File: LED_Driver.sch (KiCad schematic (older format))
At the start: 0 parts

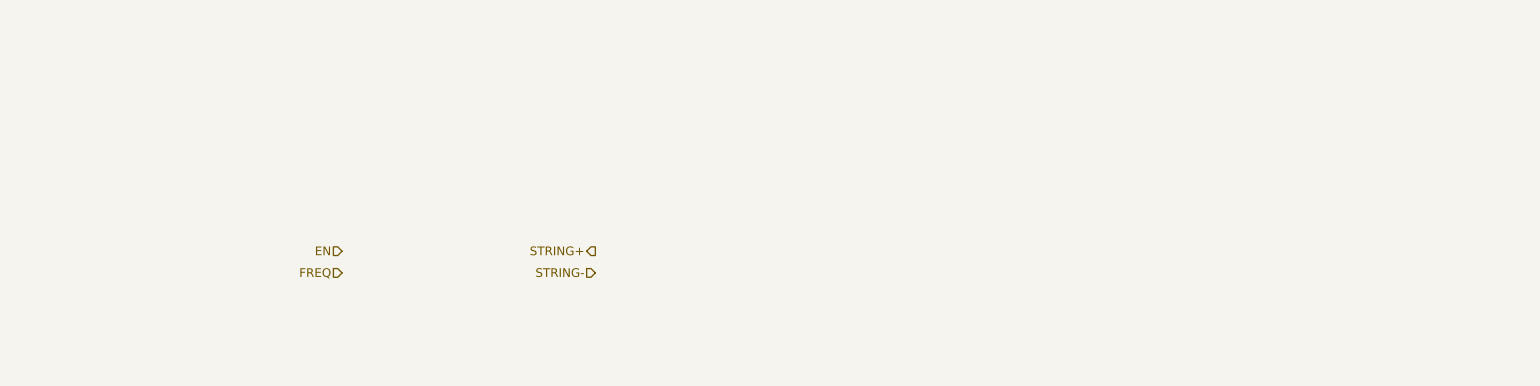
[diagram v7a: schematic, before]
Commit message: WIRED BLOCK DIAGRAM TOGETHER AND ADDED ARDUINO BLOCK
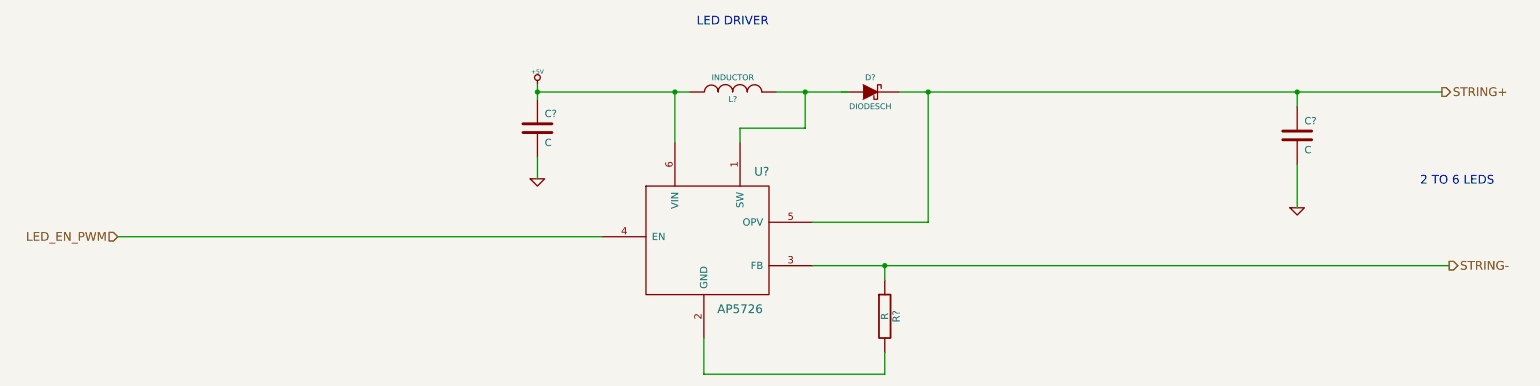
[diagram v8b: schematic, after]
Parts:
- added C? (x2): C, symbol C
- added D?: DIODESCH, symbol DIODESCH
- added L?: INDUCTOR, symbol INDUCTOR
- added R?: R, symbol R
- added U?: AP5726, symbol AP5726
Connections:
- net labels added: +5V, GND, LED_EN_PWM
- net labels removed: EN, FREQ
- wire segments 0 -> 19
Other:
- note added: "2 TO 6 LEDS\n"
- note added: "LED DRIVER"
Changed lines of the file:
@@
-EESchema Schematic File Version 2  date Sat 08 Feb 2014 08:25:16 PM EST
+EESchema Schematic File Version 2  date Sat 08 Feb 2014 11:37:49 PM EST
 LIBS:power
 LIBS:device
@@
 $Descr A4 11700 8267
 encoding utf-8
-Sheet 3 9
+Sheet 2 9
 Title ""
 Date "9 feb 2014"
@@
 Comment4 ""
 $EndDescr
-Text HLabel 4750 3450 0    60   Input ~ 0
+Text Notes 10450 2850 0    60   ~ 0
+2 TO 6 LEDS\n
+Text Notes 5450 1750 0    60   ~ 0
+LED DRIVER
+Wire Wire Line
+	9600 2700 9600 3000
+Connection ~ 6750 3400
+Wire Wire Line
+	6750 3500 6750 3400
+Connection ~ 9600 2200
+Wire Wire Line
+	10600 2200 6850 2200
+Wire Wire Line
+	6250 3100 7050 3100
+Wire Wire Line
+	7050 3100 7050 2200
+Connection ~ 5300 2200
+Wire Wire Line
+	5400 2200 4350 2200
+Connection ~ 4350 2200
+Wire Wire Line
+	5300 2200 5300 2550
+Wire Wire Line
+	4350 2650 4350 2800
+Wire Wire Line
+	1450 3200 4800 3200
+Wire Wire Line
+	4350 2150 4350 2250
+Wire Wire Line
+	5750 2550 5750 2450
+Wire Wire Line
+	5750 2450 6200 2450
+Wire Wire Line
+	6200 2450 6200 2200
+Wire Wire Line
+	6500 2200 6000 2200
+Connection ~ 6200 2200
+Wire Wire Line
+	9600 2200 9600 2300
+Connection ~ 7050 2200
+Wire Wire Line
+	6250 3400 10650 3400
+Wire Wire Line
+	6750 4000 6750 4150
+Wire Wire Line
+	6750 4150 5500 4150
+Wire Wire Line
+	5500 4150 5500 3900
+$Comp
+L C C?
+U 1 1 52F6E658
+P 9600 2500
+F 0 "C?" H 9650 2600 50  0000 L CNN
+F 1 "C" H 9650 2400 50  0000 L CNN
+	1    9600 2500
+	1    0    0    -1
+$EndComp
+$Comp
+L R R?
+U 1 1 52F6E64C
+P 6750 3750
+F 0 "R?" V 6830 3750 50  0000 C CNN
+F 1 "R" V 6750 3750 50  0000 C CNN
+	1    6750 3750
+	1    0    0    -1
+$EndComp
+$Comp
+L GND #PWR?
+U 1 1 52F6E636
+P 9600 3000
+F 0 "#PWR?" H 9600 3000 30  0001 C CNN
+F 1 "GND" H 9600 2930 30  0001 C CNN
+	1    9600 3000
+	1    0    0    -1
+$EndComp
+$Comp
+L DIODESCH D?
+U 1 1 52F6E615
+P 6650 2200
+F 0 "D?" H 6650 2300 40  0000 C CNN
+F 1 "DIODESCH" H 6650 2100 40  0000 C CNN
+	1    6650 2200
+	1    0    0    -1
+$EndComp
+$Comp
+L INDUCTOR L?
+U 1 1 52F6E5E4
+P 5700 2200
+F 0 "L?" V 5650 2200 40  0000 C CNN
+F 1 "INDUCTOR" V 5800 2200 40  0000 C CNN
+	1    5700 2200
+	0    -1   -1   0
+$EndComp
+$Comp
+L C C?
+U 1 1 52F6E5B2
+P 4350 2450
+F 0 "C?" H 4400 2550 50  0000 L CNN
+F 1 "C" H 4400 2350 50  0000 L CNN
+	1    4350 2450
+	1    0    0    -1
+$EndComp
+$Comp
+L GND #PWR?
+U 1 1 52F6E59D
+P 4350 2800
+F 0 "#PWR?" H 4350 2800 30  0001 C CNN
+F 1 "GND" H 4350 2730 30  0001 C CNN
+	1    4350 2800
+	1    0    0    -1
+$EndComp
+$Comp
+L +5V #PWR?
+U 1 1 52F6E57D
+P 4350 2150
+F 0 "#PWR?" H 4350 2240 20  0001 C CNN
+F 1 "+5V" H 4350 2240 30  0000 C CNN
+	1    4350 2150
+	1    0    0    -1
+$EndComp
+$Comp
+L AP5726 U?
+U 1 1 52F6E451
+P 5500 3200
+F 0 "U?" H 5900 3650 60  0000 C CNN
+F 1 "AP5726" H 5750 2700 60  0000 C CNN
+	1    5500 3200
+	1    0    0    -1
+$EndComp
+Text HLabel 10650 3400 2    60   Output ~ 0
 STRING-
-Text HLabel 4750 3300 0    60   Output ~ 0
+Text HLabel 10600 2200 2    60   Output ~ 0
 STRING+
-Text HLabel 3000 3450 0    60   Input ~ 0
-FREQ
-Text HLabel 3000 3300 0    60   Input ~ 0
-EN
+Text HLabel 1450 3200 0    60   Input ~ 0
+LED_EN_PWM
 $EndSCHEMATC
